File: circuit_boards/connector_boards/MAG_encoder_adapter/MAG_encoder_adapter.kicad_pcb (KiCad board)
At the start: 2 copper layers, 31.1 x 29.8 mm, 6 parts, among them J2 POT, J3 RIO

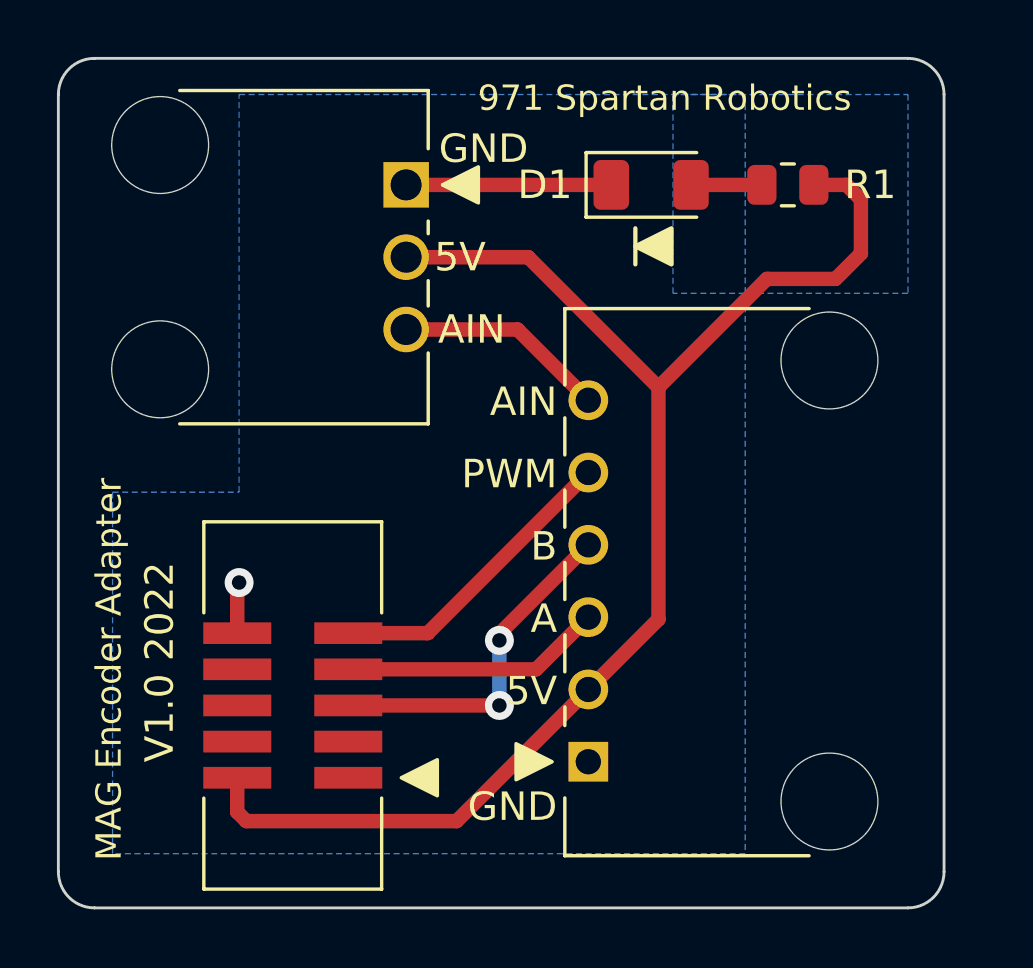
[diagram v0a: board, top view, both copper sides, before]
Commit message: Fix mag encoder board
Signed-off-by: Henry Speiser <henry@speiser.net>
Change-Id: Ibd00abfba0a6230b25acf3f77c01d51ace0d4a3c
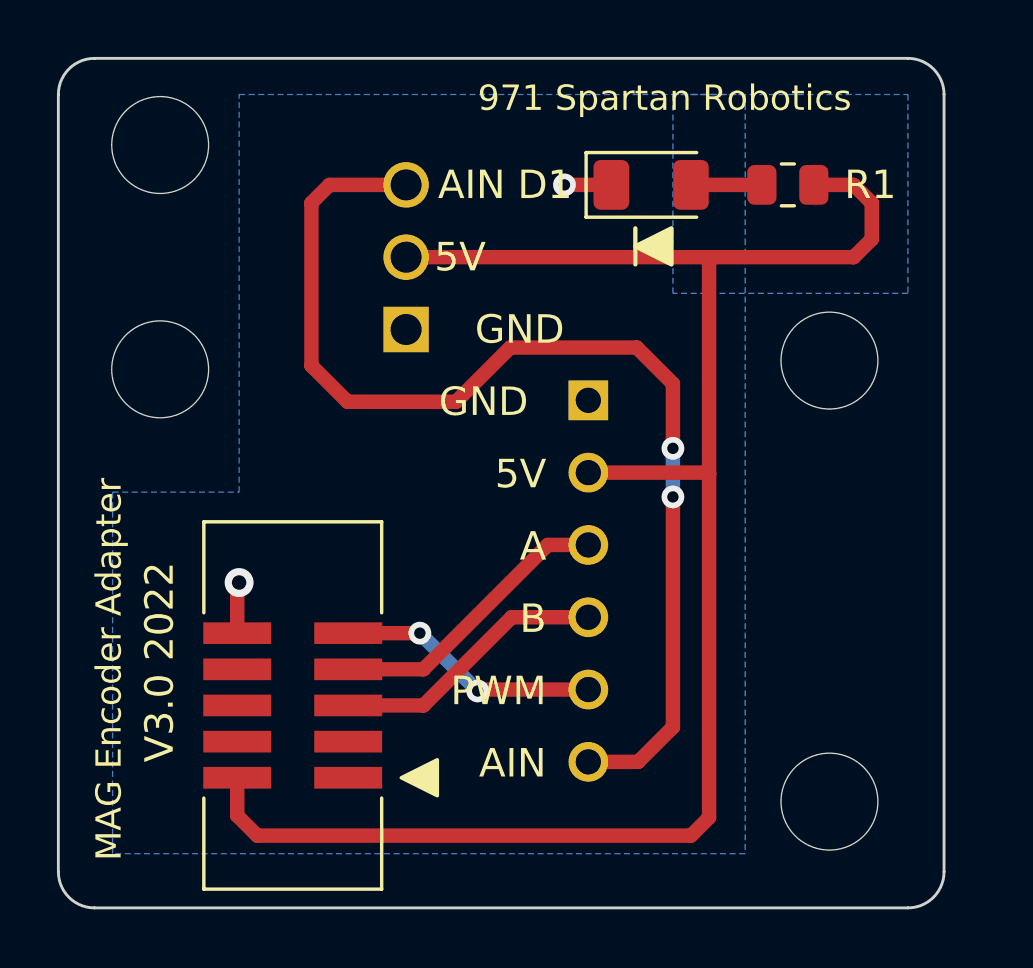
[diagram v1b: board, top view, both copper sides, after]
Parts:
- J2: moved to B.Cu
- J3: footprint MAG-encoder:0705550005 -> mag:705550005; moved to B.Cu
- moved J3 12.7 mm to (173.6, 111.7), turned to -90 degrees
- moved J2 5.08 mm to (167.2, 109.2), turned to 90 degrees
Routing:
- net /AIN: track 7.43 -> 39.4 mm, vias 0 -> 2
- net +5V: track 50.8 -> 62.6 mm
- net GND: track 9.01 -> 3.45 mm, vias 1 -> 2
- net /B: track 12.2 -> 9.72 mm, vias 2 -> 0
- net /PWM: track 10.8 -> 9.30 mm, vias 0 -> 2
- net /A: track 9.19 -> 10.2 mm
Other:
- board text added: "V3.0 2022"
- board text removed: "V1.0 2022"
